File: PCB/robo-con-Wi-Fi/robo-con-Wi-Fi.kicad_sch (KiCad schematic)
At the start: 95 parts, among them J1 Conn_01x04, J2 SMA-J, J3 Conn_01x05, J5 Conn_01x02, J7 Conn_01x06, SW1 SW_Push, SW2 SW_Push, U1 STM32H723VGTx, U10 MCP73831-2-OT, U11 LM66100DCK, U12 NJM12877, U13 TXB0606DYYR, U18 USB_Type-C, U2 LBEE5HY2FY, U3 TXU0204, U4 IS25LP128-JBLE, U5 RKJXV122400R, U6 NJM2884U1-33, U7 RKJXV122400R, U8 TMHU28, U9 TMHU28

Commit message: RF部の配線
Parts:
- removed C26: 0.33u, Capacitor_SMD:C_0402_1005Metric_Pad0.74x0.62mm_HandSolder, symbol Device:C_Small
- removed C29: 2.2u, Capacitor_SMD:C_0402_1005Metric_Pad0.74x0.62mm_HandSolder, symbol Device:C_Small
- removed R79: 1k, Resistor_SMD:R_0402_1005Metric_Pad0.72x0.64mm_HandSolder, symbol Device:R
- removed U6: NJM2884U1-33, Package_TO_SOT_SMD:SOT-89-5, symbol My_Library:NJM2884U1-33
- added C32: 0.1uF, Capacitor_SMD:C_0402_1005Metric_Pad0.74x0.62mm_HandSolder, symbol Device:C
- added D4: MS18F, Diode_SMD:D_2010_5025Metric_Pad1.52x2.65mm_HandSolder, symbol Device:D_Small
- added J4, J6: Conn_01x01, Connector_Wire:SolderWirePad_1x01_SMD_1.5x3mm, symbol Connector_Generic:Conn_01x01
- added R51, R52: WA04X102, My_Library:WA04X102, symbol My_Library:WA04X102
- added U14: TPS628513DRLR, Package_TO_SOT_SMD:SOT-583-8, symbol My_Library:TPS628513DRLR
- added U17: (no value), My_Library:ECS-TXO-2520-33-500-AN-TR, symbol My_Library:ECS-TXO-2520-33-500-AN-TR
- J1: footprint Connector_PinSocket_2.54mm:PinSocket_1x04_P2.54mm_Vertical -> Connector_PinSocket_2.54mm:PinSocket_1x04_P2.54mm_Horizontal
- J2: footprint Connector_Coaxial:SMA_Samtec_SMA-J-P-H-ST-EM1_EdgeMount -> My_Library:SMA_Conn
- R12: footprint Resistor_SMD:R_0603_1608Metric_Pad0.98x0.95mm_HandSolder -> Resistor_SMD:R_0402_1005Metric_Pad0.72x0.64mm_HandSolder
- R24: footprint Resistor_SMD:R_0402_1005Metric_Pad0.72x0.64mm_HandSolder -> Resistor_SMD:R_0603_1608Metric_Pad0.98x0.95mm_HandSolder
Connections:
- net +1V8: now also C84.1, U3.11 (VCCB), R51.1, R51.2, R51.3, R51.4, R52.1, R52.2, R52.3; no longer C85.1, U3.1 (VCCA), U3.12 (OE)
- net +3.3V: now also C85.1, U3.1 (VCCA), U3.12 (OE), C32.1, U17.1 (Tri_state), U17.4 (VDD); no longer C84.1, U3.11 (VCCB)
- net +5V: now also D4.1 (K), J4.1 (Pin_1)
- net +BATT: now also D4.2 (A)
- net GND: now also C32.2, J6.1 (Pin_1), U17.2 (GND)
- net SDMMC1_CLK: now also U1.80 (PC12)
- net SDMMC1_CMD: now also U1.83 (PD2), U13.11 (B5); no longer U13.14 (B2)
- net SDMMC1_D0: now also U1.65 (PC8), U13.10 (B6); no longer U13.13 (B3)
- net SDMMC1_D1: now also U1.66 (PC9)
- net SDMMC1_D2: now also U1.78 (PC10), U13.13 (B3); no longer U13.11 (B5)
- net SDMMC1_D3: now also U1.79 (PC11), U13.14 (B2); no longer U13.10 (B6)
- net Wi-Fi_CMD: now also U13.6 (A5); no longer U13.3 (A2)
- net Wi-Fi_D0: now also U13.7 (A6); no longer U13.4 (A3)
- net Wi-Fi_D2: now also U13.4 (A3); no longer U13.6 (A5)
- net Wi-Fi_D3: now also U13.3 (A2); no longer U13.7 (A6)
- net OSC: now reaches U1.12 (PH0)
- net OSC: now also U17.3 (Output)
- net WL-GPIO_6: now reaches U2.1 (GPIO_6)
- net WL-GPIO_6: now also R51.5
- net WL-GPIO_0: now reaches U2.2 (GPIO_0)
- net WL-GPIO_0: now also R51.6
- net WL-GPIO_3: now reaches U2.3 (GPIO_3)
- net WL-GPIO_3: now also R51.7
- net WL-GPIO_5: now reaches U2.4 (GPIO_5)
- net WL-GPIO_5: now also R51.8
- net LHL_GPIO_1: now reaches U2.5 (LHL_GPIO_1)
- net LHL_GPIO_1: now also R52.5
- net WL-GPIO_4: now reaches U2.6 (GPIO_4)
- net WL-GPIO_4: now also R52.6
- net WL-GPIO_2: now reaches U2.7 (GPIO_2)
- net WL-GPIO_2: now also R52.7
- net ST_LED_W5500 renamed ST_LED_BOOT
- no-connect marks 14 -> 21
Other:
- note added: "BT"
- note added: "Level Shifter"
- note added: "Wi-Fi"
- note added: "external falsh"
- moved on the sheet: C62, C63, C75, C76, C77, C78, C79, C80, C81, C82, C83, C84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

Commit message: 電源周りの部品構成完了
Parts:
- removed D4: MS18F, Diode_SMD:D_2010_5025Metric_Pad1.52x2.65mm_HandSolder, symbol Device:D_Small
- removed R35, R36: 1k, Resistor_SMD:R_0402_1005Metric_Pad0.72x0.64mm_HandSolder, symbol Device:R_Small
- removed R51, R52: WA04X102, My_Library:WA04X102, symbol My_Library:WA04X102
- removed U4: IS25LP128-JBLE, Package_SO:SOIC-8_5.3x5.3mm_P1.27mm, symbol My_Library:IS25LP128-JBLE
- added C14, C15: 0.1u, Capacitor_SMD:C_0402_1005Metric_Pad0.74x0.62mm_HandSolder, symbol Device:C_Small
- added C88, C89, C91, C92: 10u, Capacitor_SMD:C_0603_1608Metric_Pad1.08x0.95mm_HandSolder, symbol Device:C_Small
- added C90, C95: 2.2u, Capacitor_SMD:C_0402_1005Metric_Pad0.74x0.62mm_HandSolder, symbol Device:C_Small
- added C93: 1u, Capacitor_SMD:C_0402_1005Metric_Pad0.74x0.62mm_HandSolder, symbol Device:C_Small
- added C94: 10p, Capacitor_SMD:C_0402_1005Metric_Pad0.74x0.62mm_HandSolder, symbol Device:C_Small
- added L2: 0.47u, Inductor_SMD:L_0603_1608Metric_Pad1.05x0.95mm_HandSolder, symbol Device:L
- added Q1: 2SC3325-Y, Package_TO_SOT_SMD:SC-59, symbol My_Library:2SC3325-Y
- added R3: 2.2k, Resistor_SMD:R_0402_1005Metric_Pad0.72x0.64mm_HandSolder, symbol Device:R_Small
- added R39: 10k, Resistor_SMD:R_0402_1005Metric_Pad0.72x0.64mm_HandSolder, symbol Device:R_Small
- added R40: 88.7k, Resistor_SMD:R_0402_1005Metric_Pad0.72x0.64mm_HandSolder, symbol Device:R_Small
- added R41: 19.6k, Resistor_SMD:R_0402_1005Metric_Pad0.72x0.64mm_HandSolder, symbol Device:R_Small
- added R42: 100k, Resistor_SMD:R_0402_1005Metric_Pad0.72x0.64mm_HandSolder, symbol Device:R_Small
- added U15: LM66100DCK, Package_TO_SOT_SMD:SOT-363_SC-70-6, symbol Power_Management:LM66100DCK
- added U4: MCP1792x-3302xCB, Package_TO_SOT_SMD:SOT-23, symbol Regulator_Linear:MCP1792x-3302xCB
- added U6: IS25LP064D-JLLE, Package_SON:WSON-8-1EP_8x6mm_P1.27mm_EP3.4x4.3mm, symbol My_Library:IS25LP064D
- L1: footprint Capacitor_SMD:C_0402_1005Metric_Pad0.74x0.62mm_HandSolder -> Inductor_SMD:L_1008_2520Metric_Pad1.43x2.20mm_HandSolder
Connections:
- net +3.3V: now also C91.1, C92.1, C94.1, L2.2, Q1.3 (C), R40.1, R42.1, U6.8 (Vcc); no longer C32.1, U17.1 (Tri_state), U17.4 (VDD)
- net +5V: now also U14.1 (VIN), U14.2 (EN), U14.3 (MODE), C15.1, C88.1, C89.1, C90.1, U15.6 (VOUT), U4.3 (VI)
- net +BATT: now also C14.1, U15.1 (VIN)
- net GND: now also U14.8 (GND), C14.2, C15.2, C88.2, C89.2, C90.2, C91.2, C92.2, C93.2, C95.2, R39.2, R41.2, U15.2 (GND), U15.3 (~{CE}), U15.5 (ST), U4.1 (GND), U6.4 (GND), U6.9 (GND)
- net UART1_CTS: now also U1.84 (PD3)
- net UART1_RTS: now also U1.85 (PD4)
- net UART1_RX: now also U1.87 (PD6)
- net UART1_TX: now also U1.86 (PD5)
- net Wi-Fi_CLK: now also R3.1
- net SPI1_MOSI/QSPI1_IO0: now reaches U1.15 (PC0)
- net SPI1_MOSI/QSPI1_IO0: now also U6.5 (SI(IO0))
- net SPI1_MISO/QSPI1_IO1: now reaches U1.16 (PC1)
- net SPI1_MISO/QSPI1_IO1: now also U6.2 (SO(IO1))
- net WP/QSPI1_IO2: now reaches U1.17 (PC2_C)
- net WP/QSPI1_IO2: now also U6.3 (WP(IO2))
- net SPI1_SCK/QSPI1_SCK: now reaches U1.25 (PA3)
- net SPI1_SCK/QSPI1_SCK: now also U6.6 (SCK)
- net HOLD/QSPI1_IO3: now reaches U1.40 (PE10)
- net HOLD/QSPI1_IO3: now also U6.7 (HOLD/RESET(IO3))
- net SPI1_NSS/QSPI1_NSS: now reaches U1.41 (PE11)
- net SPI1_NSS/QSPI1_NSS: now also U6.1 (CE#)
- net SDMMC1_CLKIN: now reaches U1.95 (PB8)
- net SDMMC1_CLKIN: now also Q1.2 (E), R39.1
- net BT_HOST_WAKE: now reaches U2.41 (BT_HOST_WAKE)
- net BT_DEV_WAKE: now reaches U2.40 (LHL_GPIO_0)
- net at U14.4 (SS/TR): now also C93.1
- net at U14.5 (FB): now also C94.2, R40.2, R41.1
- net at U14.6 (PG): now also R42.2
- net at U14.7 (SW): now also L2.1
- net LHL_GPIO_1 renamed WL_DEV_WAKE
- net WL-GPIO_0 renamed WL_HOST_WAKE
- net WL-GPIO_2: no longer names the net of U2.7 (GPIO_2)
- net WL-GPIO_3: no longer names the net of U2.3 (GPIO_3)
- net WL-GPIO_4: no longer names the net of U2.6 (GPIO_4)
- net WL-GPIO_5: no longer names the net of U2.4 (GPIO_5)
- net WL-GPIO_6: no longer names the net of U2.1 (GPIO_6)
- new net: Q1.1 (B), R3.2
- new net OSC_3.3v: C32.1, C95.1, U17.1 (Tri_state), U17.4 (VDD), U4.2 (VO)
- no-connect marks 21 -> 24
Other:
- moved on the sheet: C32, C82, C83, C86, C87, R12, U13

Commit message: PCB
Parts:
- removed C32: 0.1uF, Capacitor_SMD:C_0402_1005Metric_Pad0.74x0.62mm_HandSolder, symbol Device:C
- removed C90, C95: 2.2u, Capacitor_SMD:C_0402_1005Metric_Pad0.74x0.62mm_HandSolder, symbol Device:C_Small
- removed U17: (no value), My_Library:ECS-TXO-2520-33-500-AN-TR, symbol My_Library:ECS-TXO-2520-33-500-AN-TR
- removed U4: MCP1792x-3302xCB, Package_TO_SOT_SMD:SOT-23, symbol Regulator_Linear:MCP1792x-3302xCB
- added C34, C35: 18pF, Capacitor_SMD:C_0402_1005Metric_Pad0.74x0.62mm_HandSolder, symbol Device:C_Small
- added R43: 1k, Resistor_SMD:R_0402_1005Metric_Pad0.72x0.64mm_HandSolder, symbol Device:R_Small
- added Y2: XRCGB25M000FFS1AR0, My_Library:XRCGB25M000FFS1AR0, symbol My_Library:XRCGB25M000FFS1AR0
- R23: footprint Resistor_SMD:R_0603_1608Metric_Pad0.98x0.95mm_HandSolder -> Resistor_SMD:R_0402_1005Metric_Pad0.72x0.64mm_HandSolder
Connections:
- net BT_UART_CTS: now also U3.9 (B2Y); no longer U3.7 (B4)
- net BT_UART_RTS: now also U3.7 (B4); no longer U3.8 (B3)
- net BT_UART_RX: now also U3.10 (B1Y); no longer U3.9 (B2Y)
- net BT_UART_TX: now also U3.8 (B3); no longer U3.10 (B1Y)
- net GND: now also C34.2, C35.2, R43.2
- net UART1_CTS: now also U3.5 (A4Y); no longer U3.4 (A3Y)
- net UART1_RTS: now also U3.3 (A2); no longer U3.5 (A4Y)
- net UART1_RX: now also U3.4 (A3Y); no longer U3.2 (A1)
- net UART1_TX: now also U3.2 (A1); no longer U3.3 (A2)
- net HSE_OUT: now reaches U1.13 (PH1)
- net HSE_OUT: now also C34.1, Y2.1
- net BT_DEV_WAKE: no longer names the net of U2.40 (LHL_GPIO_0)
- net BT_DEV_WAKE: now also R43.1
- net BT_HOST_WAKE: no longer names the net of U2.41 (BT_HOST_WAKE)
- net OSC renamed HSE_IN
- net HSE_IN: now also C35.1, Y2.3 (2)
- net ST_LED_0 renamed LED_0
- net ST_LED_1 renamed LED_1
- net ST_LED_2 renamed LED_2
- net ST_LED_3 renamed LED_3
- net ST_LED_4 renamed LED_4
- net ST_LED_BOOT renamed LED_Wi-Fi
- net ST_LED_USB renamed LED_USB
- net WL_DEV_WAKE: no longer names the net of U2.5 (LHL_GPIO_1)
- net WL_HOST_WAKE: no longer names the net of U2.2 (GPIO_0)
- no-connect marks 24 -> 26

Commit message: LiPo監視用ADCとLED追加
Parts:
- added D16: R, Diode_SMD:D_0603_1608Metric_Pad1.05x0.95mm_HandSolder, symbol Device:LED_Small
- added D17: G, Diode_SMD:D_0603_1608Metric_Pad1.05x0.95mm_HandSolder, symbol Device:LED_Small
- added R35, R36: 1k, Resistor_SMD:R_0402_1005Metric_Pad0.72x0.64mm_HandSolder, symbol Device:R_Small
- added R5, R8: 22, Resistor_SMD:R_0402_1005Metric_Pad0.72x0.64mm_HandSolder, symbol Device:R_Small
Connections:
- net +3.3V: now also D17.2 (A)
- net GND: now also D16.1 (K)
- net USB_DFU_DN: now also R5.2; no longer U18.A7 (D-), U18.B7 (D-)
- net USB_DFU_DP: now also R8.2; no longer U18.A6 (D+), U18.B6 (D+)
- net LiPo_Observer: now reaches F1.1, J5.1 (Pin_1)
- new net: R8.1, U18.A6 (D+), U18.B6 (D+)
- new net: D17.1 (K), R36.1
- new net: D16.2 (A), R35.2
- new net: R5.1, U18.A7 (D-), U18.B7 (D-)
- new net LiPo_State: R35.1, R36.2
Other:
- moved on the sheet: F1, U18

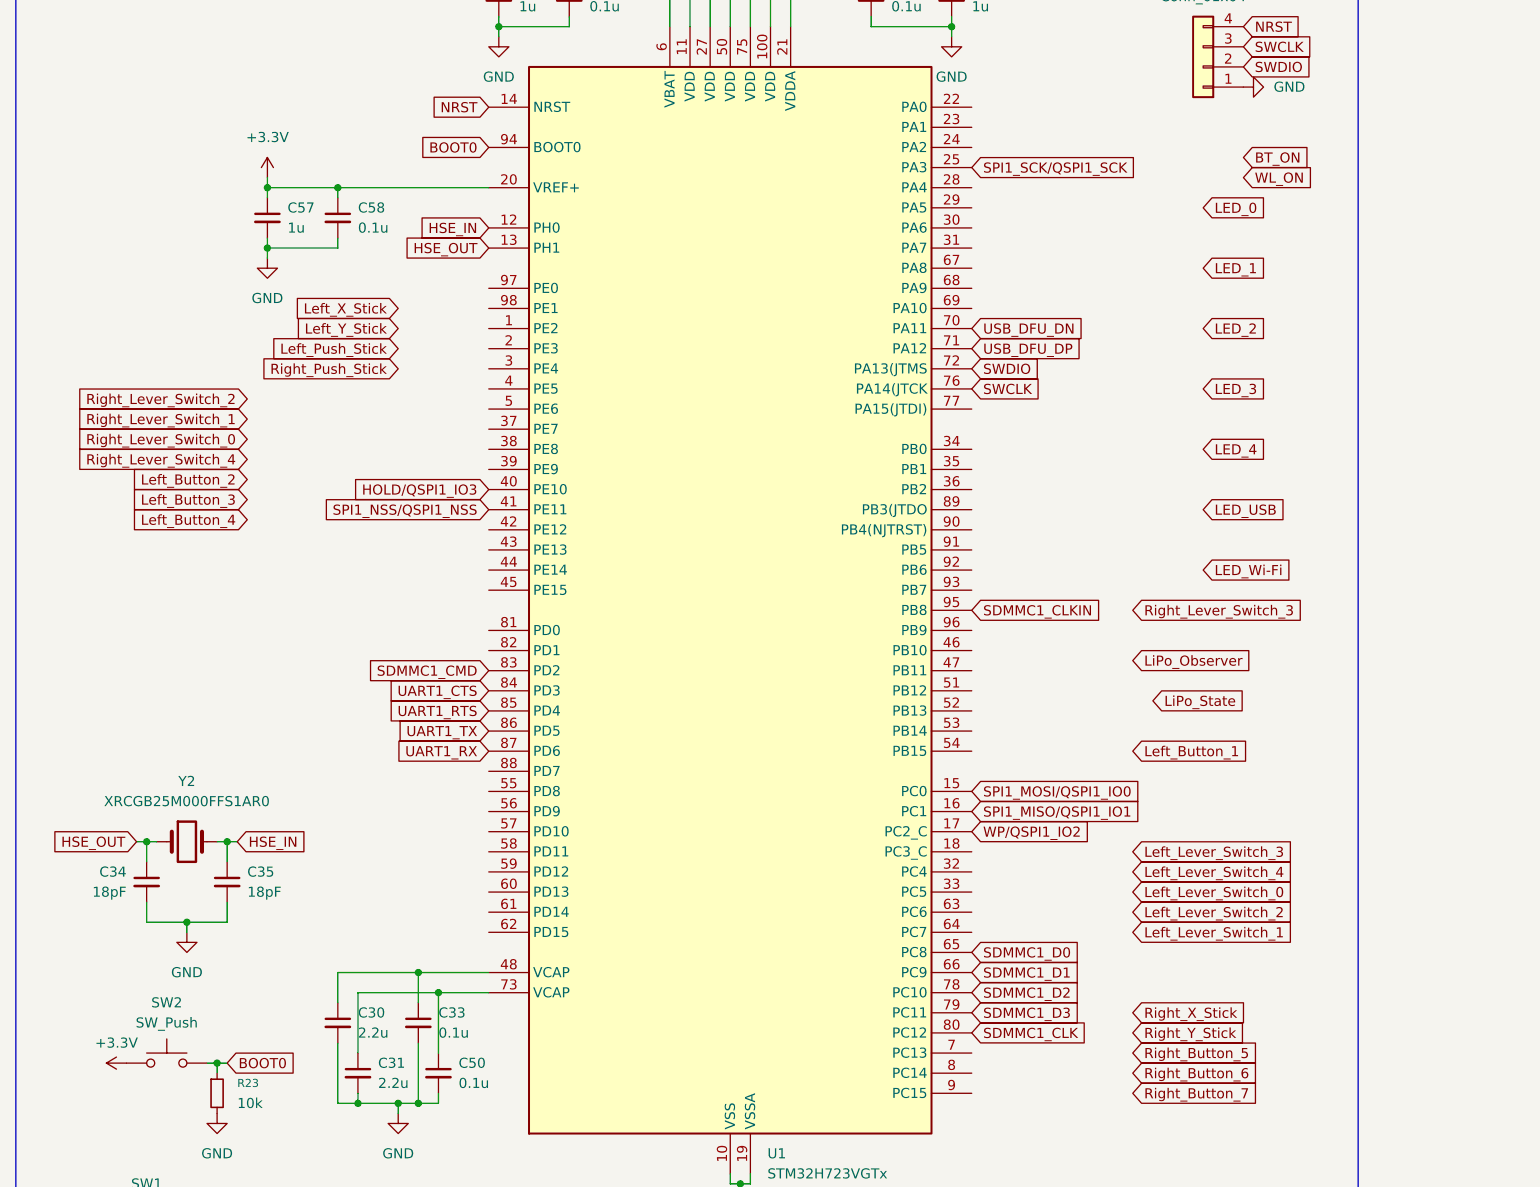
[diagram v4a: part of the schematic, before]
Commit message: フットプリントを配置残り配線と配線長合わせ
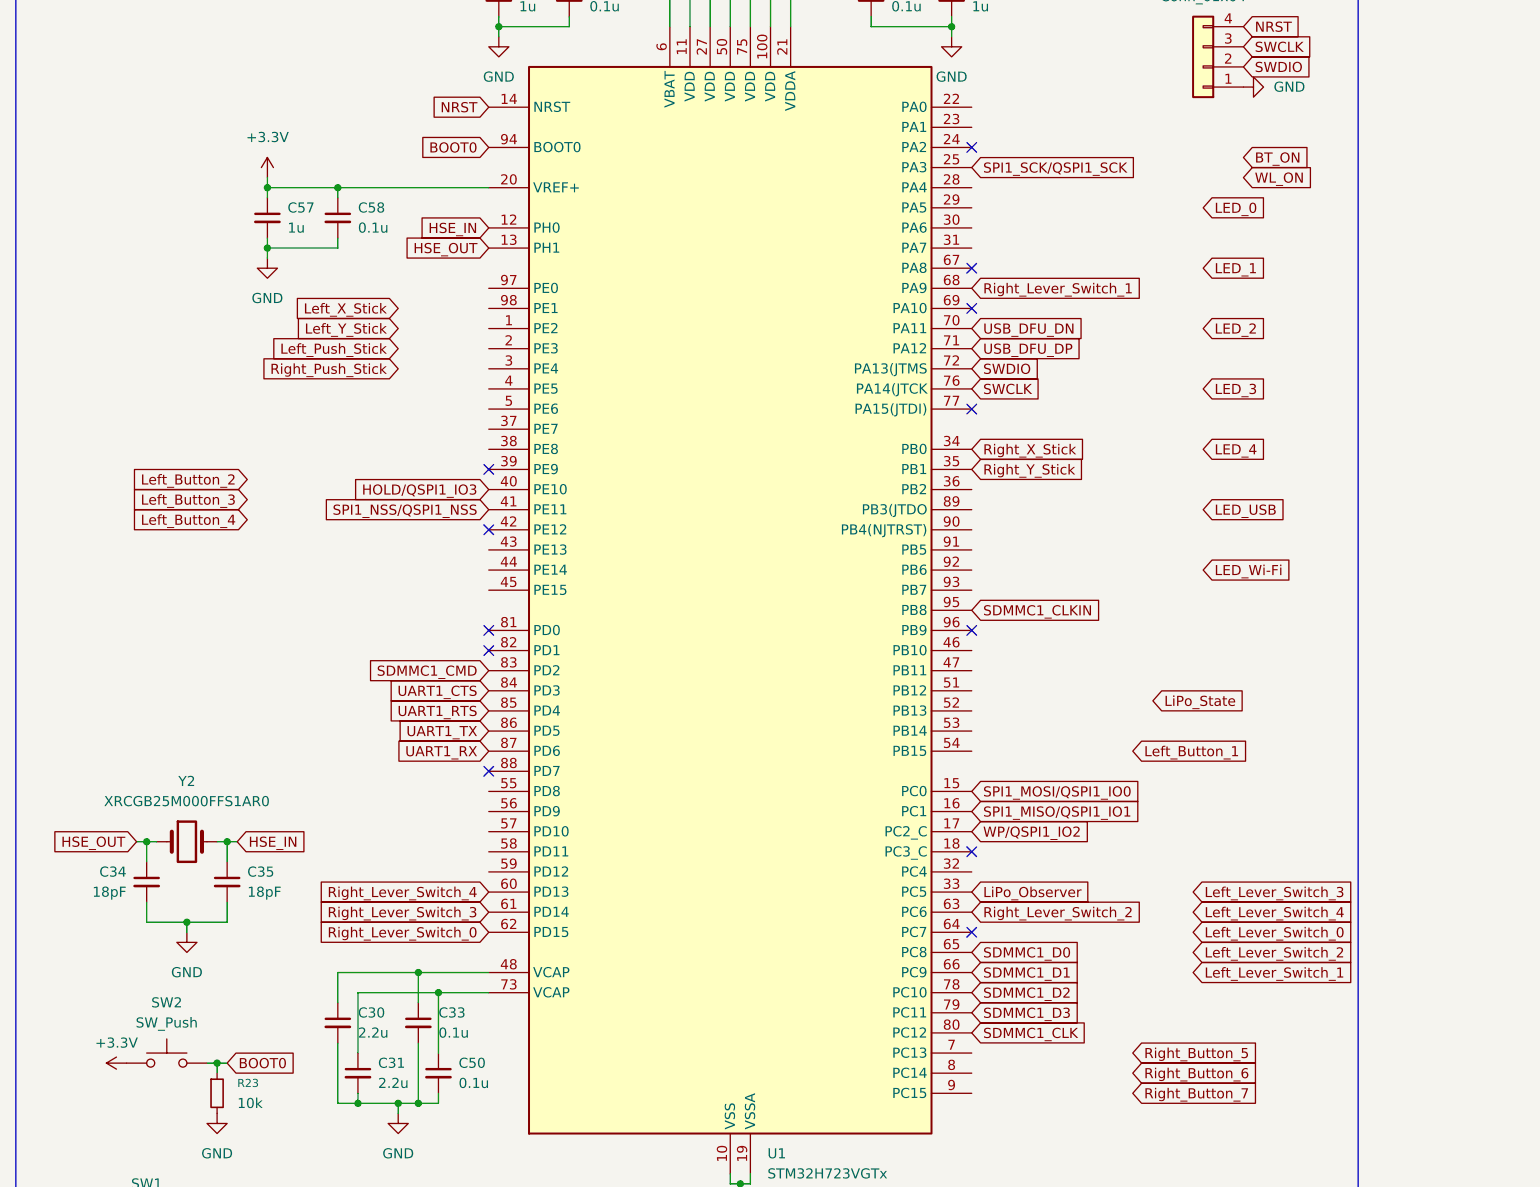
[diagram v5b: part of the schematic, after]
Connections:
- net LiPo_Observer: now also U1.33 (PC5)
- net Right_Lever_Switch_0: now also U1.62 (PD15)
- net Right_Lever_Switch_1: now also U1.68 (PA9)
- net Right_Lever_Switch_2: now also U1.63 (PC6)
- net Right_Lever_Switch_3: now also U1.61 (PD14)
- net Right_Lever_Switch_4: now also U1.60 (PD13)
- net Right_X_Stick: now also U1.34 (PB0)
- net Right_Y_Stick: now also U1.35 (PB1)
- no-connect marks 26 -> 38

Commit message: PCB配線した　長さ合わせた後確認
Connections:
- net BT_ON: now also U1.92 (PB6)
- net LED_0: now also U1.30 (PA6)
- net LED_1: now also U1.31 (PA7)
- net LED_2: now also U1.32 (PC4)
- net LED_3: now also U1.36 (PB2)
- net LED_4: now also U1.37 (PE7)
- net LED_USB: now also U1.28 (PA4)
- net LED_Wi-Fi: now also U1.29 (PA5)
- net Left_Button_1: now also U1.51 (PB12)
- net Left_Button_2: now also U1.52 (PB13)
- net Left_Button_3: now also U1.53 (PB14)
- net Left_Button_4: now also U1.54 (PB15)
- net Left_Lever_Switch_0: now also U1.3 (PE4)
- net Left_Lever_Switch_1: now also U1.1 (PE2)
- net Left_Lever_Switch_2: now also U1.2 (PE3)
- net Left_Lever_Switch_3: now also U1.5 (PE6)
- net Left_Lever_Switch_4: now also U1.4 (PE5)
- net Left_Push_Stick: now also U1.46 (PB10)
- net Left_X_Stick: now also U1.23 (PA1)
- net Left_Y_Stick: now also U1.22 (PA0)
- net LiPo_State: now also U1.47 (PB11)
- net Right_Button_5: now also U1.43 (PE13)
- net Right_Button_6: now also U1.44 (PE14)
- net Right_Button_7: now also U1.45 (PE15)
- net Right_Push_Stick: now also U1.38 (PE8)
- net WL_ON: now also U1.93 (PB7)

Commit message: ほぼ完成
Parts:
- added R26, R27: 1k, Resistor_SMD:R_0603_1608Metric_Pad0.98x0.95mm_HandSolder, symbol Device:R_Small
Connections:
- net GND: now also R26.2
- net LiPo_Observer: now also R26.1, R27.2; no longer F1.1, J5.1 (Pin_1)
- new net: F1.1, J5.1 (Pin_1), R27.1
- no-connect marks 38 -> 51
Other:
- moved on the sheet: F1, J5
